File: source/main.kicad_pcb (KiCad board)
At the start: 2 copper layers, 85.6 x 54 mm, 44 parts, among them P1 USB_Type_C_Receptacle_16_pin

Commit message: Fix GR_Text
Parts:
- added D20: LED, lcsc:LED0402-R-RD_RED, F.Cu at (53.8, 34.0)
- added R22: 100Ω, lcsc:R0402, F.Cu at (54.9, 34.0)
- moved D10 20.4 mm to (53.8, 40.0)
- moved R10 20.4 mm to (54.9, 40.0)
- moved D16 15.5 mm to (45.8, 34.0)
- moved R16 15.5 mm to (46.9, 34.0)
- moved D15 15.4 mm to (45.8, 36.0)
- moved R15 15.4 mm to (46.9, 36.0)
- moved D5 15.3 mm to (47.8, 34.0)
- moved R5 15.3 mm to (48.9, 34.0)
- moved D14 15.2 mm to (45.8, 38.0)
- moved R14 15.2 mm to (46.9, 38.0)
- moved D4 15.2 mm to (47.8, 36.0)
- moved R4 15.2 mm to (48.9, 36.0)
- moved D7 15.1 mm to (49.8, 34.0)
- moved R7 15.1 mm to (50.9, 34.0)
- moved D13 15.0 mm to (45.8, 40.0)
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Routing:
- net D20-1-R22-1: track 0.00 -> 1.12 mm
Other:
- board text added: "PixelCard"

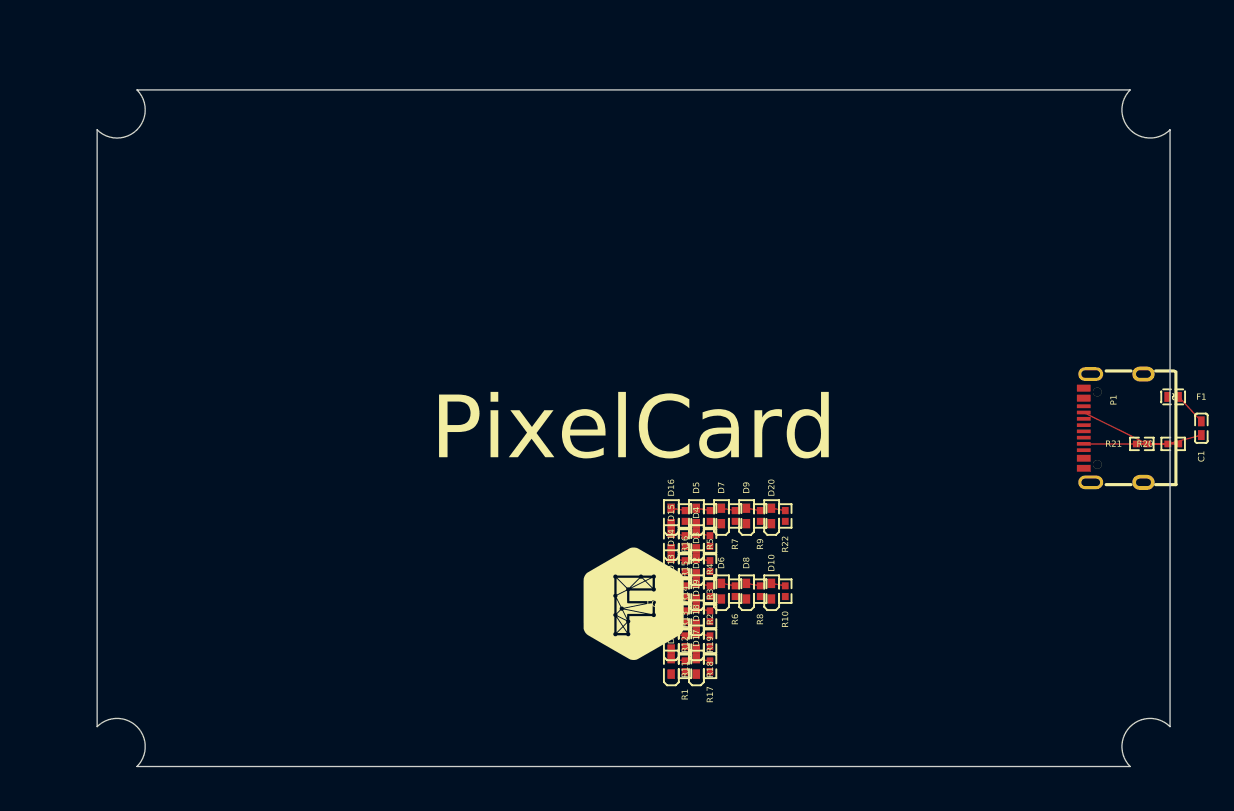
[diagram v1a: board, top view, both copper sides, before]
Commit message: Update component placement
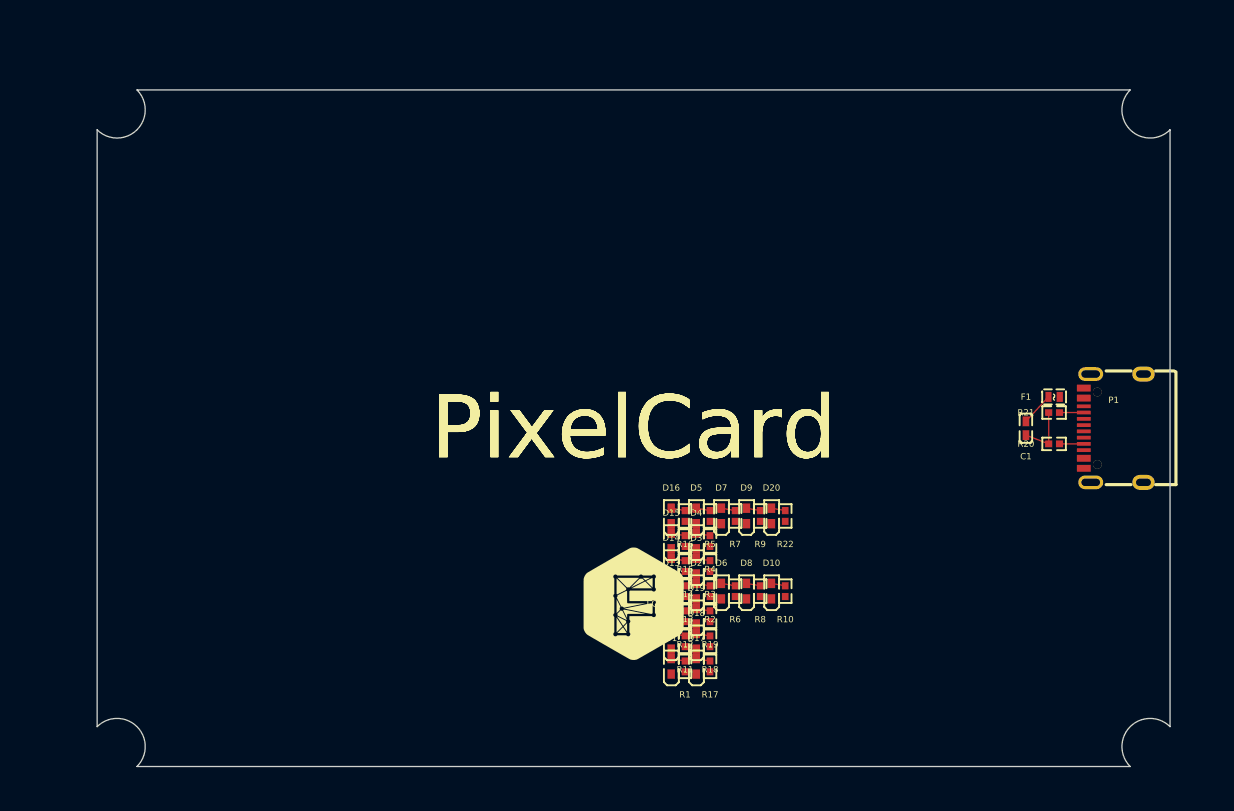
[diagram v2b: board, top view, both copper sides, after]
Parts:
- moved C1 14.0 mm to (74.1, 27.0)
- moved F1 9.50 mm to (76.3, 24.5), turned to 180 degrees
- moved R20 9.50 mm to (76.3, 28.2)
- moved R21 7.43 mm to (76.3, 25.7)
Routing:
- net P1-4-R20-1: track 7.56 -> 1.94 mm
- net P1-9-R21-1: track 5.64 -> 1.94 mm
- net gnd: track 5.27 -> 4.45 mm

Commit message: Basic vias
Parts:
- removed D10, D18, D19, D20, D3, D6, D7, D8, D9: LED, lcsc:LED0402-R-RD_RED
- removed R10, R18, R19, R22, R3, R6, R7, R8, R9: 100Ω, lcsc:R0402
- moved R2 8.84 mm to (55.1, 33.7)
- moved D2 8.66 mm to (54.0, 34.0)
- moved D5 8.47 mm to (54.0, 39.7)
- moved R5 8.30 mm to (55.1, 39.5)
- moved R17 7.54 mm to (52.6, 39.5)
- moved D17 7.32 mm to (51.5, 39.7)
- moved D15 4.94 mm to (49.0, 39.7)
- moved R15 4.75 mm to (50.1, 39.5)
- moved R4 4.37 mm to (52.6, 33.7)
- moved R14 4.32 mm to (47.6, 33.7)
- moved D4 4.25 mm to (51.5, 34.0)
- moved D14 4.07 mm to (46.5, 34.0)
- moved R13 3.47 mm to (47.6, 36.6)
- moved R16 3.26 mm to (50.1, 33.7)
- moved D16 3.25 mm to (49.0, 34.0)
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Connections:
- D1 pad 2: D1-2 -> vbus
- D11 pad 2: D11-2 -> vbus
- D12 pad 2: D12-2 -> vbus
- D13 pad 2: D13-2 -> vbus
- D14 pad 2: D14-2 -> vbus
- D15 pad 2: D15-2 -> vbus
- D16 pad 2: D16-2 -> vbus
- D17 pad 2: D17-2 -> vbus
- D2 pad 2: D2-2 -> vbus
- D4 pad 2: D4-2 -> vbus
- D5 pad 2: D5-2 -> vbus
- R1 pad 2: R1-2 -> gnd
- R11 pad 2: R11-2 -> gnd
- R12 pad 2: R12-2 -> gnd
- R13 pad 2: R13-2 -> gnd
- R14 pad 2: R14-2 -> gnd
- R15 pad 2: R15-2 -> gnd
- R16 pad 2: R16-2 -> gnd
- R17 pad 2: R17-2 -> gnd
- R2 pad 2: R2-2 -> gnd
- R4 pad 2: R4-2 -> gnd
- R5 pad 2: R5-2 -> gnd
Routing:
- net vbus: track 2.65 -> 22.2 mm, vias 0 -> 13
- net gnd: track 4.45 -> 0.00 mm
- net P1-9-R21-1: track 1.94 -> 3.88 mm
- net P1-4-R20-1: track 1.94 -> 3.88 mm
- net D9-1-R9-1: track 1.12 -> 0.00 mm
- net D8-1-R8-1: track 1.12 -> 0.00 mm
- net D7-1-R7-1: track 1.12 -> 0.00 mm
- net D6-1-R6-1: track 1.12 -> 0.00 mm
- net D3-1-R3-1: track 1.12 -> 0.00 mm
- net D20-1-R22-1: track 1.12 -> 0.00 mm
- net D19-1-R19-1: track 1.12 -> 0.00 mm
- net D18-1-R18-1: track 1.12 -> 0.00 mm
- net D10-1-R10-1: track 1.12 -> 0.00 mm
- net D5-1-R5-1: track 1.12 -> 2.20 mm
- net D4-1-R4-1: track 1.12 -> 2.20 mm
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- added copper zone on F.Cu, net gnd
- added copper zone on B.Cu, net vbus

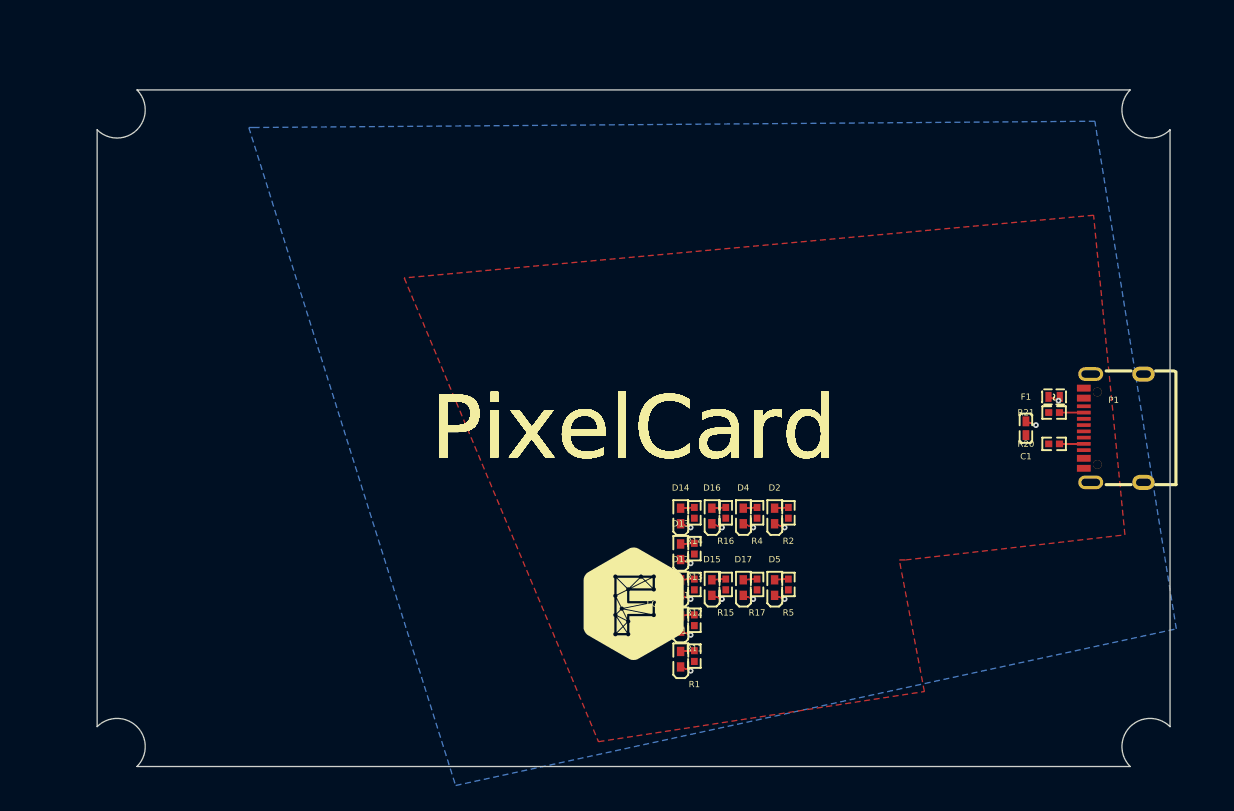
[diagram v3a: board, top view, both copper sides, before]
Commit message: Improved reso & moved net routing
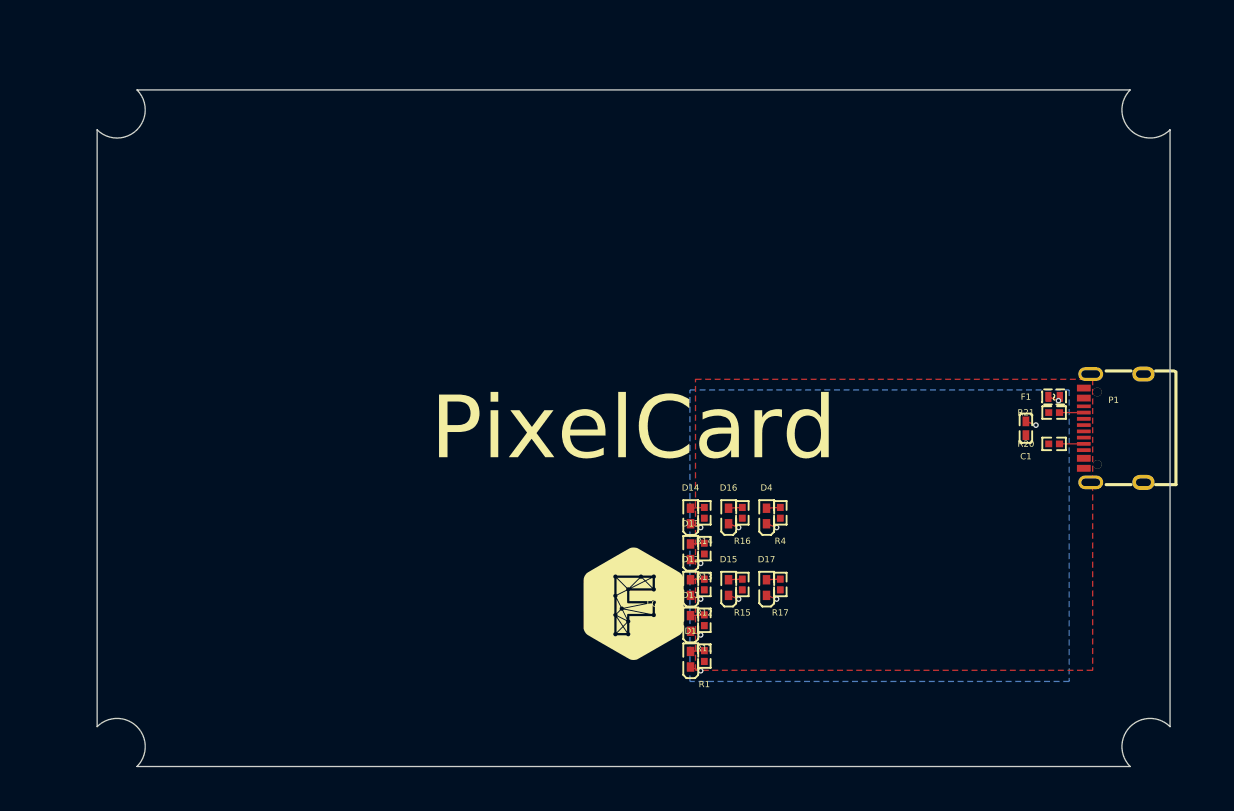
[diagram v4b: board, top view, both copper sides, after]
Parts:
- removed D2, D5: LED, lcsc:LED0402-R-RD_RED
- removed R2, R5: 100Ω, lcsc:R0402
- moved D17 1.86 mm to (53.4, 39.7)
- moved D4 1.86 mm to (53.4, 34.0)
- moved R17 1.86 mm to (54.5, 39.5)
- moved R4 1.86 mm to (54.5, 33.7)
- moved D15 1.33 mm to (50.4, 39.7)
- moved D16 1.33 mm to (50.4, 34.0)
- moved R15 1.33 mm to (51.5, 39.5)
- moved R16 1.33 mm to (51.5, 33.7)
- moved D1 0.80 mm to (47.3, 45.4)
- moved D11 0.80 mm to (47.3, 42.6)
- moved D12 0.80 mm to (47.3, 39.7)
- moved D13 0.80 mm to (47.3, 36.8)
- moved D14 0.80 mm to (47.3, 34.0)
- moved R1 0.80 mm to (48.4, 45.2)
- moved R11 0.80 mm to (48.4, 42.3)
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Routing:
- net vbus: track 22.2 -> 9.40 mm, vias 13 -> 11
- net D5-1-R5-1: track 2.20 -> 0.00 mm
- net D2-1-R2-1: track 2.20 -> 0.00 mm
- net P1-9-R21-1: track 3.88 -> 1.94 mm
- net P1-4-R20-1: track 3.88 -> 1.94 mm
- net D16-1-R16-1: track 2.20 -> 1.10 mm
- net D15-1-R15-1: track 2.20 -> 1.10 mm
- net D4-1-R4-1: track 2.20 -> 1.10 mm
- net D17-1-R17-1: track 2.20 -> 1.10 mm
- net D14-1-R14-1: track 2.20 -> 1.10 mm
- net D13-1-R13-1: track 2.20 -> 1.10 mm
- net D12-1-R12-1: track 2.20 -> 1.10 mm
- net D11-1-R11-1: track 2.20 -> 1.10 mm
- net D1-1-R1-1: track 2.20 -> 1.10 mm

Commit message: Contact info & Some params
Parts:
- added D10: LED, lcsc:LED0402-R-RD_RED, F.Cu at (31.2, 11.4)
- added D18: LED, lcsc:LED0402-R-RD_RED, F.Cu at (31.2, 8.57)
- added D19: LED, lcsc:LED0402-R-RD_RED, F.Cu at (31.2, 5.71)
- added D2: LED, lcsc:LED0402-R-RD_RED, F.Cu at (18.6, 8.57)
- added D20: LED, lcsc:LED0402-R-RD_RED, F.Cu at (31.2, 2.86)
- added D21: LED, lcsc:LED0402-R-RD_RED, F.Cu at (34.2, 14.3)
- added D22: LED, lcsc:LED0402-R-RD_RED, F.Cu at (34.2, 11.4)
- added D23: LED, lcsc:LED0402-R-RD_RED, F.Cu at (34.2, 0.00)
- added D24: LED, lcsc:LED0402-R-RD_RED, F.Cu at (37.3, 14.3)
- added D25: LED, lcsc:LED0402-R-RD_RED, F.Cu at (37.3, 11.4)
- added D26: LED, lcsc:LED0402-R-RD_RED, F.Cu at (37.3, 8.57)
- added D27: LED, lcsc:LED0402-R-RD_RED, F.Cu at (37.3, 5.71)
- added D28: LED, lcsc:LED0402-R-RD_RED, F.Cu at (37.3, 2.86)
- added D29: LED, lcsc:LED0402-R-RD_RED, F.Cu at (40.3, 17.1)
- added D3: LED, lcsc:LED0402-R-RD_RED, F.Cu at (15.6, 0.00)
- added D30: LED, lcsc:LED0402-R-RD_RED, F.Cu at (40.3, 14.3)
- added D5: LED, lcsc:LED0402-R-RD_RED, F.Cu at (18.6, 5.71)
- added D6: LED, lcsc:LED0402-R-RD_RED, F.Cu at (18.6, 0.00)
- added D7: LED, lcsc:LED0402-R-RD_RED, F.Cu at (28.2, 17.1)
- added D8: LED, lcsc:LED0402-R-RD_RED, F.Cu at (28.2, 14.3)
- added D9: LED, lcsc:LED0402-R-RD_RED, F.Cu at (31.2, 14.3)
- added R10: 100Ω, lcsc:R0402, F.Cu at (32.3, 11.2)
- added R18: 100Ω, lcsc:R0402, F.Cu at (32.3, 8.32)
- added R19: 100Ω, lcsc:R0402, F.Cu at (32.3, 5.46)
- added R2: 100Ω, lcsc:R0402, F.Cu at (19.7, 8.32)
- added R22: 100Ω, lcsc:R0402, F.Cu at (32.3, 2.61)
- added R23: 100Ω, lcsc:R0402, F.Cu at (35.3, 14.0)
- added R24: 100Ω, lcsc:R0402, F.Cu at (35.3, 11.2)
- added R25: 100Ω, lcsc:R0402, F.Cu at (35.3, -0.25)
- added R26: 100Ω, lcsc:R0402, F.Cu at (38.4, 14.0)
- added R27: 100Ω, lcsc:R0402, F.Cu at (38.4, 11.2)
- added R28: 100Ω, lcsc:R0402, F.Cu at (38.4, 8.32)
- added R29: 100Ω, lcsc:R0402, F.Cu at (38.4, 5.46)
- added R3: 100Ω, lcsc:R0402, F.Cu at (16.7, -0.25)
- added R30: 100Ω, lcsc:R0402, F.Cu at (38.4, 2.61)
- added R31: 100Ω, lcsc:R0402, F.Cu at (41.4, 16.9)
- added R32: 100Ω, lcsc:R0402, F.Cu at (41.4, 14.0)
- added R5: 100Ω, lcsc:R0402, F.Cu at (19.7, 5.46)
- added R6: 100Ω, lcsc:R0402, F.Cu at (19.7, -0.25)
- added R7: 100Ω, lcsc:R0402, F.Cu at (29.3, 16.9)
- added R8: 100Ω, lcsc:R0402, F.Cu at (29.3, 14.0)
- added R9: 100Ω, lcsc:R0402, F.Cu at (32.3, 14.0)
- moved D15 52.8 mm to (12.6, 2.86)
- moved R15 52.8 mm to (13.7, 2.61)
- moved D16 50.8 mm to (12.6, 0.00)
- moved R16 50.8 mm to (13.7, -0.25)
- moved D17 49.0 mm to (15.6, 8.57)
- moved R17 49.0 mm to (16.7, 8.32)
- moved D4 47.2 mm to (15.6, 5.71)
- moved R4 47.2 mm to (16.7, 5.46)
- moved D1 44.8 mm to (12.6, 17.1)
- moved D12 44.8 mm to (12.6, 11.4)
- moved D13 44.8 mm to (12.6, 8.57)
- moved D14 44.8 mm to (12.6, 5.71)
- moved R1 44.8 mm to (13.7, 16.9)
- moved R12 44.8 mm to (13.7, 11.2)
- moved R13 44.8 mm to (13.7, 8.32)
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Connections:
- D1 pad 2: vbus -> D1-2
- D11 pad 2: vbus -> D11-2
- D12 pad 2: vbus -> D12-2
- D13 pad 2: vbus -> D13-2
- D14 pad 2: vbus -> D14-2
- D15 pad 2: vbus -> D15-2
- D16 pad 2: vbus -> D16-2
- D17 pad 2: vbus -> D17-2
- D4 pad 2: vbus -> D4-2
- R1 pad 2: gnd -> R1-2
- R11 pad 2: gnd -> R11-2
- R12 pad 2: gnd -> R12-2
- R13 pad 2: gnd -> R13-2
- R14 pad 2: gnd -> R14-2
- R15 pad 2: gnd -> R15-2
- R16 pad 2: gnd -> R16-2
- R17 pad 2: gnd -> R17-2
- R4 pad 2: gnd -> R4-2
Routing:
- net vbus: track 9.40 -> 1.71 mm, vias 11 -> 2
- net D9-1-R9-1: track 0.00 -> 1.10 mm
- net D8-1-R8-1: track 0.00 -> 1.10 mm
- net D7-1-R7-1: track 0.00 -> 1.10 mm
- net D30-1-R32-1: track 0.00 -> 1.10 mm
- net D3-1-R3-1: track 0.00 -> 1.10 mm
- net D29-1-R31-1: track 0.00 -> 1.10 mm
- net D23-1-R25-1: track 0.00 -> 1.10 mm
- net D22-1-R24-1: track 0.00 -> 1.10 mm
- net D21-1-R23-1: track 0.00 -> 1.10 mm
- net D20-1-R22-1: track 0.00 -> 1.10 mm
- net D19-1-R19-1: track 0.00 -> 1.10 mm
- net D18-1-R18-1: track 0.00 -> 1.10 mm
- net D10-1-R10-1: track 0.00 -> 1.10 mm
- net D6-1-R6-1: track 0.00 -> 1.10 mm
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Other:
- board text added: "FA"
- board text added: "Name: ABC"
- board text added: "Tel: 0612341234"
- board text added: "Url: github.com"
- board text removed: "PixelCard"
